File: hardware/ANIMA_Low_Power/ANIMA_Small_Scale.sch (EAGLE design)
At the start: 61 parts, among them J1 POW_CONNECTFEMALE-RA, Q1 MOSFET-PCHANNELSMD, Q2 MOSFET-PCHANNELSMD, Q3 MOSFET-PCHANNELSMD, Q4 MOSFET-PCHANNELSMD, Q5 MOSFET-PCHANNELSMD, Q6 MOSFET-PCHANNELSMD, U1 PIC32MX20FB-44PIN, U12 MICRO-SDCARDSOCKET, U2 TPS54040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

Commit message: creation of package for new processor replaced high power with low and reconnected major connections
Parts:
- removed C1: .1u, ANIMAlib:CAP0805
- removed C2: 47p, ANIMAlib:CAP0805
- removed C3: .018u, ANIMAlib:CAP0805
- removed C4: .015u, ANIMAlib:CAP0805
- removed C8: 10u, ANIMAlib:CAP1206
- removed D1: (no value), ANIMAlib:DIODE-ZENER1
- removed L1: 68uH, ANIMAlib:INDUCTORELL-CTVV
- removed R3: 15.8K, ANIMAlib:RESISTOR0805-RES
- removed R4: 165K, ANIMAlib:RESISTOR0805-RES
- removed R5: 31.6K, ANIMAlib:RESISTOR0805-RES
- removed R6: 10K, ANIMAlib:RESISTOR0805-RES
- removed U2: TPS54040, ANIMAlib:TPS54040
- U1: value PIC32MX20FB-44PIN -> PIC24FJXXXGA204-44PIN; device ANIMAlib:PIC32MX20FB-44PIN -> ANIMAlib:PIC24FJXXXGA204-44PIN
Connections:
- removed net N$10: R5.1, R6.2, U2.VSENSE
- removed net N$14: R4.2, U2.RT/CLK
- removed net N$15: C4.2, U2.SS/TR
- removed net N$5: C1.1, D1.C, L1.1, U2.PH
- removed net N$6: C2.1, C3.2, R3.1
- removed net N$8: R3.2, U2.COMP
- new net N$24: C5.2, Q2.S
- net ACCEL_POWER_EN: now also U1PORTA.RA2/OSCI/CLKI/CN30; no longer U1PORTA.OSC1/CLKI/CN30/RA2
- net CD1: now also U1PORTB.RB4/SOSCI/RPI4/CN1; no longer U1PORTB.SOSCI/RP4/CN1/RB4
- net CD2: now also U1PORTC.RC9/RP26/CN19; no longer U1PORTC.RPC9/CTED7/PMA6/RC9
- net DEBUG_RX: now also U1PORTC.RC5/RP21/CN28; no longer U1PORTC.RPC5/PMA3/RC5
- net DEBUG_TX: now also U1PORTC.RC3/RP319/CN28; no longer U1PORTC.RPC3/RC3
- net DLED1: now also U1PORTB.RB5/PGED3/ASDA1/RP5/CN27; no longer U1PORTB.TMS/RP5/USBID/RB5
- net DLED2: now also U1PORTB.RB7/RP7/INT0/CN23; no longer U1PORTB.TDI/RP7/INT0/RB7
- net DLED3: now also U1PORTB.RB9/RP9/SDA1/CN21; no longer U1PORTB.TDO/RP9/SDA1/RB9
- net DLED4: now also U1PORTB.RB8/RP8/SCL1/CN22; no longer U1PORTB.TCK/RP8/SCL1/RB8
- net GND: no longer C2.2, C3.1, C4.1, C8.2, D1.A, R4.1, R6.1, U2.GND
- net GPS_EN: now also U1PORTA.RA10/TMS/CN36; no longer U1PORTA.PGED/PMA10/RA10
- net GPS_POWER: now also U1PORTA.RA7/TCK/CN33; no longer U1PORTA.PGEC/CTED8/PMA7/RA7
- net GPS_RX: now also U1PORTB.RB10/PGED2/RP10/CN16; no longer U1PORTB.PGED2/RP10/D+/RB10
- net GPS_TX: now also U1PORTB.RB11/PGEC2/RP11/CN15; no longer U1PORTB.PGEC2/RP11/D-/RB11
- net I2C_POWER_EN: now also U1PORTC.RC0/AN10/RP16/CN8; no longer U1PORTC.AN6/RPC0/RC0
- net MAG3110_INT: now also U1PORTA.RA8/TDI/CN34; no longer U1PORTA.RPA8/PMA8/RA8
- net MAG_POWER_EN: now also U1PORTA.RA3/OSCO/CLKO/CN29; no longer U1PORTA.OSC2/CLKO/CN29/RA3
- net MISO: now also U1PORTC.RC6/RP22/CN18; no longer U1PORTC.RPC6/PMA1/RC6
- net MMA8451_INT1: now also U1PORTC.RC2/AN12/RP18/CN10; no longer U1PORTC.AN8/RPC2/PMA2/RC2
- net MMA8451_INT2: now also U1PORTC.RC1/AN11/RP17/CN9; no longer U1PORTC.AN7/RPC1/RC1
- net MOSI: now also U1PORTC.RC8/RP24/CN29; no longer U1PORTC.RPC8/PMA5/RC8
- net N$4: now also U1PORTA.RA4/SOSCO/CN0; no longer C1.2, U2.BOOT
- net PGEC: now also U1PORTB.RB1/PGEC1/AN3/RP1/CN5; no longer U1PORTB.PGEC1/AN3/RP1/CN5/RB1
- net PGED: now also U1PORTB.RB0/PGED1/AN2/RP0/CN4; no longer U1PORTB.PGED1/AN2/RP0/CN4/RB0
- net SCK: now also U1PORTB.RB15/AN9/RP15/CN11; no longer U1PORTB.AN9/RP15/SCK2/RB15
- net SCL: now also U1PORTB.RB3/AN5/RP3/SCL2/CN7; no longer U1PORTB.AN5/RP3/SCL2/CN7/RB3
- net SDA: now also U1PORTB.RB2/AN4/RP2/SDA2/CN6; no longer U1PORTB.AN4/RP2/SDA2/CN6/RB2
- net SD_POWER_EN: now also U1PORTA.RA1/AN1/VREF-/CN3; no longer U1PORTA.AN1/VREF-/CN3/RA1
- net SS: now also U1PORTB.RB14/AN06/RP14/RTCC/CN12; no longer U1PORTB.AN10//RP14/SCK1/RB14
- net TEMPERATURE: now also U1PORTA.RA0/AN0/VREF+/CN2; no longer U1PORTA.AN0/VREF+/CN2/RA0
- net VBAT: no longer C5.2, Q2.S, U2.VIN
- net VBAT_SCALED: now also U1PORTB.RB13/AN07/RP13/CN13; no longer U1PORTB.AN11/RPB13/RB13
- net VCC3V3: no longer C8.1, L1.2, R5.2, U1POWER.VUSB3V3

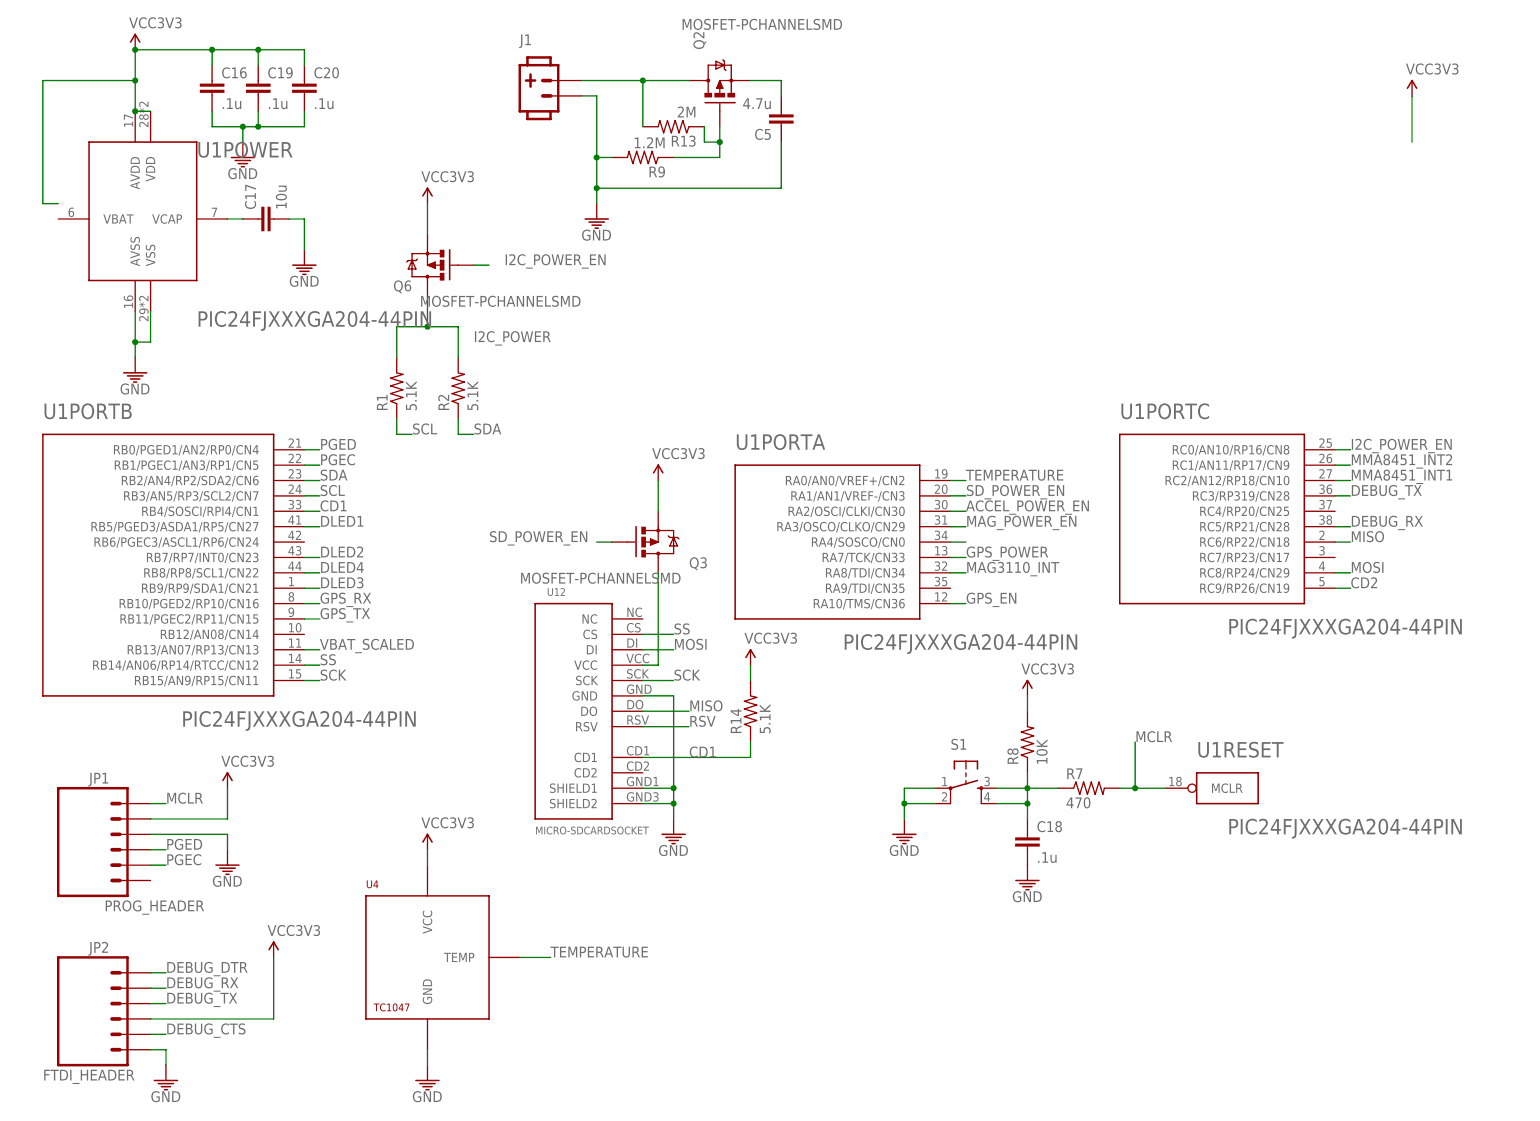
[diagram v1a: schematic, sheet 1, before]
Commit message: added oscillator removed connections prior to moving GPS to new position added additional parts
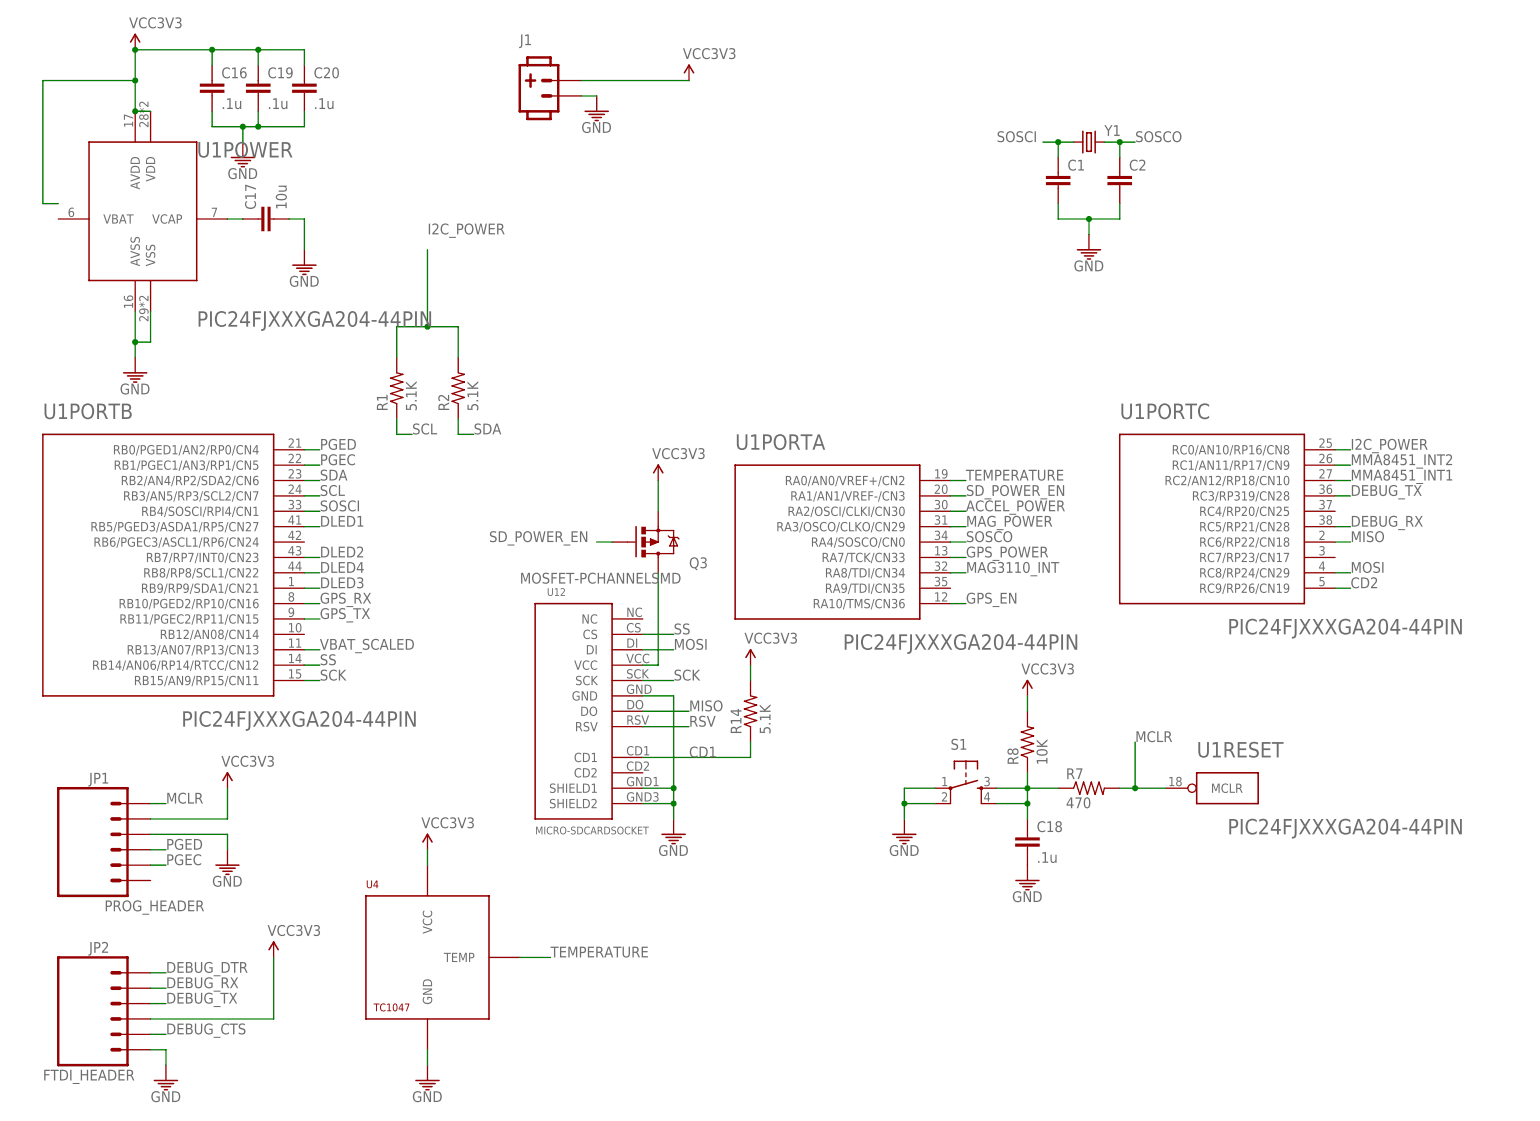
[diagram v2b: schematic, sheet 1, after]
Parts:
- removed C5: 4.7u, ANIMAlib:CAP0805
- removed Q2, Q4, Q5, Q6: MOSFET-PCHANNELSMD, ANIMAlib:MOSFET-PCHANNELSMD
- removed R11: 30K, ANIMAlib:RESISTOR0805-RES
- removed R12: 7.5K, ANIMAlib:RESISTOR0805-RES
- removed R13: 2M, ANIMAlib:RESISTOR0805-RES
- removed R9: 1.2M, ANIMAlib:RESISTOR0805-RES
- added C1, C2: (no value), ANIMAlib:CAP0805
- added Y1: (no value), ANIMAlib:CRYSTALABS07
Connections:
- removed net ACCEL_POWER_EN: Q4.G, U1PORTA.RA2/OSCI/CLKI/CN30
- removed net I2C_POWER_EN: Q6.G, U1PORTC.RC0/AN10/RP16/CN8
- removed net MAG_POWER_EN: Q5.G, U1PORTA.RA3/OSCO/CLKO/CN29
- removed net N$12: Q2.G, R13.1, R9.1
- removed net N$20: J1.1, Q2.D, R13.2
- removed net N$24: C5.2, Q2.S
- removed net N$4: U1PORTA.RA4/SOSCO/CN0
- removed net VBAT: R11.2
- new net SOSCI: C1.1, U1PORTB.RB4/SOSCI/RPI4/CN1, Y1.1
- new net SOSCO: C2.1, U1PORTA.RA4/SOSCO/CN0, Y1.2
- net ACCEL_POWER: now also U1PORTA.RA2/OSCI/CLKI/CN30; no longer Q4.D
- net CD1: no longer U1PORTB.RB4/SOSCI/RPI4/CN1
- net GND: now also C1.2, C2.2; no longer C5.1, R12.1, R9.2
- net I2C_POWER: now also U1PORTC.RC0/AN10/RP16/CN8; no longer Q6.D
- net MAG_POWER: now also U1PORTA.RA3/OSCO/CLKO/CN29; no longer Q5.D
- net VBAT_SCALED: no longer R11.1, R12.2
- net VCC3V3: now also J1.1; no longer Q4.S, Q5.S, Q6.S
